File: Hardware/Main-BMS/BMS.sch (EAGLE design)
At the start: 131 parts, among them IC2 TLC6C5912-Q1, J1 SL03THROUGH_HOLE, J2 SL03THROUGH_HOLE, Q1 2N7002PW, Q11 2N7002PW, Q12 2N7002PW, Q13 2N7002PW, Q14 2N7002PW, Q15 2N7002PW, Q2 2N7002PW, Q3 2N7002PW, X1 22-23-2021, X2 22-23-2021, X3 22-23-2021, X4 22-23-2021, X5 22-23-2041, X6 22-23-2101, X7 22-23-2101

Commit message: Changed after board review
Made all changes suggested in pcb review, including several part
additions and complete rerouting.
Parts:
- removed D17, D18: BAT46W, SparkFun-DiscreteSemi:DIODE-ZENER16V
- removed S2: SWITCH-MOMENTARY-2SMD, SparkFun-Electromechanical:SWITCH-MOMENTARY-2SMD
- removed U$14: RJ45-8PTH, SparkFun-Connectors:RJ45-8PTH
- added D2, D24: BAT46WJ, diode:DIODE-SOD323-R
- added IC1: ACS759, MRDT-ICs:ACS759
- added R33: 200R, rcl:R-US_R0805
- added S1: SWITCH-MOMENTARY-2PTH, BMS:SWITCH-MOMENTARY-2PTH
- U$1: value ACS759 -> 5PIN; device MRDT-2017-BMS:ACS759 -> Molex-SL:5PIN
- U$13: value MSP432P401R-LAUNCHPAD -> MSP430R401R; device 2016PowerPackLibraries:MSP432P401R-LAUNCHPAD -> MRDT-Microcontrollers:MSP430R401R
- U$3: value Q_LTC6803-1 -> LTC6803-1; device MRDT-2017-BMS:Q_LTC6803-1 -> MRDT-ICs:LTC6803-1
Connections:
- removed net BMS_VREF: U$3.VREF
- removed net N$12: U$13.P3.3
- new net N$7: Q1.S, R33.2
- net +3V3: now also IC1.VCC; no longer U$1.VCC
- net 5V: now also Q3.D; no longer Q3.S
- net BMS_CSBI: now also U$13.P5.4; no longer U$13.P6.2
- net BMS_SCLK: now also U$13.P5.5; no longer U$13.P6.3
- net BUZZ_1: now also U$13.P4.7; no longer U$13.P8.6
- net CELL_8: now also IC1.IP-; no longer U$1.IP-
- net GAUGE_ON: now also S1.2, U$13.P4.6; no longer S2.2, U$13.P1.5
- net GND: now also D2.A, D24.A, IC1.GND, R33.1, S1.1, U$1.5; no longer D17.A, D18.A, Q1.S, S2.1, U$1.GND, U$14.7, U$14.8
- net LED_RCK: now also U$13.P3.3; no longer U$13.P6.1
- net LED_SER_IN: now also U$13.P1.5; no longer U$13.P4.3
- net LED_SRCK: now also U$13.P4.3; no longer U$13.P3.2
- net N$26: now also D2.C, D24.C; no longer D17.C, D18.C
- net N$35: now also U$1.1; no longer U$14.1
- net N$4: now also Q3.S; no longer Q3.D
- net N$41: now also IC1.IP+; no longer U$1.IP+
- net N$45: now also U$1.2; no longer U$14.2
- net N$62: now also U$1.4; no longer U$14.6
- net N$67: now also U$1.3; no longer U$14.3
- net PACK_GATE: now also U$13.P4.4; no longer U$13.P5.2
- net PACK_I_MEAS: now also IC1.VOUT, U$13.P6.0; no longer U$1.VIOUT, U$13.P4.5
- net TEMP_2: now also U$13.P5.6; no longer U$13.P3.5
- net V_CHECK_OUT: now also U$13.P4.5; no longer U$13.P4.4
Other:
- note removed: "BMS_VREF"
- note removed: "BMS_VREG"
- note removed: "CELL_1"
- note removed: "CELL_1_BAL"
- note removed: "CELL_1_FILTER"
- note removed: "CELL_2_BAL"
- note removed: "CELL_2_FILTER"
- note removed: "CELL_3_BAL"
- note removed: "CELL_3_FILTER"
- note removed: "CELL_4_BAL"
- note removed: "CELL_4_FILTER"
- note removed: "CELL_5_BAL"
- note removed: "CELL_5_FILTER"
- note removed: "CELL_6_BAL"
- note removed: "CELL_6_FILTER"
- note removed: "CELL_7_BAL"
- note removed: "CELL_7_FILTER"
- note removed: "CELL_8_BAL"
- note removed: "CELL_8_FILTER"
- moved on the sheet: V_ARRAY

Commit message: Changes for mountability
Changed GND terminal to Anderson connector, moved to opposite corner.
Changed package for current sensor, added connector for indicator
connection, swapped all data connectors for molex SLs
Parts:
- removed CELL-IN, CELL-MEAS: 22-23-2091, con-molex:22-23-2091
- removed GAUGE_ON: M02POLAR, SparkFun-Connectors:M02POLAR
- removed V_OUT1: TERMINAL_HOLE, MRDT-2015-PowerBoard:TERMINAL_HOLE
- removed X1, X2, X3, X4: 22-23-2021, con-molex:22-23-2021
- removed X6, X7: 22-23-2101, con-molex:22-23-2101
- added D4, D6: BZT52C15-7-F, SparkFun-DiscreteSemi:DIODE-ZENER16V
- added H1, H2, H3, H4: MOUNTING_HOLE#4, MRDT-Hardware:MOUNTING_HOLE#4
- added J3: APPPP45_PCB_VERT, MRDT-Connectors:APPPP45_PCB_VERT
- added U$10, U$11: SL10, MRDT-Connectors:SL10
- added U$12, U$14: SL09, MRDT-Connectors:SL09
- added U$16, U$2, U$5, U$6, U$7: SL02-VERT, MRDT-Connectors:SL02-VERT
- added U$18: SL04, MRDT-Connectors:SL04
- C21, C22: device resistor:C-USC1206 -> rcl:C-USC0805
- J1, J2: value SL03THROUGH_HOLE -> SL03; device MRDT-Connectors:SL03THROUGH_HOLE -> MRDT-Connectors:SL03
- R20, R40: device resistor:R-US_R1206 -> rcl:R-US_R0805
- R22, R57: device rcl:R-US_R1206 -> rcl:R-US_R0805
- R29, R30, R31, R32: value 10k -> 100k; device rcl:R-US_R1206 -> rcl:R-US_R0805
- U$1: value 5PIN -> SL05; device Molex-SL:5PIN -> MRDT-Connectors:SL05
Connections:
- removed net BUZZ_2: U$13.P8.5
- removed net SUPPLY_CTL: U$13.P2.3
- removed net SUPPLY_DC_OK: U$13.P1.7
- net 5V: now also U$18.3, U$2.1, U$5.1, U$6.1, U$7.1; no longer X1-2.S, X2-2.S, X3-2.S, X4-2.S
- net CELL_1: now also U$12.2, U$14.2; no longer CELL-IN-8.S, CELL-MEAS-8.S
- net CELL_2: now also U$12.3, U$14.3; no longer CELL-IN-7.S, CELL-MEAS-7.S
- net CELL_3: now also U$12.4, U$14.4; no longer CELL-IN-6.S, CELL-MEAS-6.S
- net CELL_4: now also U$12.5, U$14.5; no longer CELL-IN-5.S, CELL-MEAS-5.S
- net CELL_5: now also U$12.6, U$14.6; no longer CELL-IN-4.S, CELL-MEAS-4.S
- net CELL_6: now also U$12.7, U$14.7; no longer CELL-IN-3.S, CELL-MEAS-3.S
- net CELL_7: now also U$12.8, U$14.8; no longer CELL-IN-2.S, CELL-MEAS-2.S
- net CELL_8: now also IC1.IP+, U$12.9, U$14.9; no longer CELL-IN-1.S, CELL-MEAS-1.S, IC1.IP-
- net GAUGE_D: now also U$10.7; no longer X6-7.S
- net GAUGE_ON: now also U$16.2; no longer GAUGE_ON.2
- net GND: now also D4.A, D6.A, J3.P$1, U$12.1, U$14.1, U$16.1, U$18.4; no longer CELL-IN-9.S, CELL-MEAS-9.S, GAUGE_ON.1, V_OUT1.P$1
- net N$10: now also D4.C
- net N$13: now also D6.C
- net N$32: now also U$10.10; no longer X6-10.S
- net N$35: now also U$1.4, U$18.2; no longer U$1.1
- net N$41: now also IC1.IP-; no longer IC1.IP+
- net N$43: now also U$10.9; no longer X6-9.S
- net N$44: now also U$10.8; no longer X6-8.S
- net N$45: now also U$1.3, U$18.1; no longer U$1.2
- net N$46: now also U$10.6; no longer X6-6.S
- net N$47: now also U$10.5; no longer X6-5.S
- net N$48: now also U$10.4; no longer X6-4.S
- net N$49: now also U$10.3; no longer X6-3.S
- net N$50: now also U$10.2; no longer X6-2.S
- net N$51: now also U$10.1; no longer X6-1.S
- net N$62: now also U$1.2; no longer U$1.4
- net N$66: now also U$2.2; no longer X1-1.S
- net N$67: now also U$1.1; no longer U$1.3
- net N$70: now also U$5.2; no longer X2-1.S
- net N$71: now also U$6.2; no longer X3-1.S
- net N$72: now also U$7.2; no longer X4-1.S
- net N$75: now also U$11.1; no longer X7-1.S
- net N$76: now also U$11.2; no longer X7-2.S
- net N$77: now also U$11.3; no longer X7-3.S
- net N$78: now also U$11.4; no longer X7-4.S
- net N$79: now also U$11.5; no longer X7-5.S
- net N$80: now also U$11.6; no longer X7-6.S
- net N$81: now also U$11.7; no longer X7-7.S
- net N$82: now also U$11.8; no longer X7-8.S
- net N$83: now also U$11.9; no longer X7-9.S
- net N$84: now also U$11.10; no longer X7-10.S
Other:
- note added: "Communications connector"
- note added: "Indicator connector"
- note removed: "BMS_CSBI"
- note removed: "BMS_MISO"
- note removed: "BMS_MOSI"
- note removed: "BMS_SCLK"
- moved on the sheet: C18, IC1, R17, R18, R19, R21, R58, R59, R60, R61, R62, R63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

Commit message: DRC error fixes
Fixed several traces changed due to moving GND, and flipped signiture to
top.
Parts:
- R40: device rcl:R-US_R0805 -> rcl:R-US_R1206
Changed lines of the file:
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@@
 <part name="GND22" library="SparkFun-Aesthetics" deviceset="GND" device=""/>
 <part name="LED1" library="SparkFun-LED" deviceset="LED" device="1206"/>
-<part name="R40" library="rcl" deviceset="R-US_" device="R0805" value="5kΩ"/>
+<part name="R40" library="rcl" deviceset="R-US_" device="R1206" value="5kΩ"/>
 <part name="GND23" library="SparkFun-Aesthetics" deviceset="GND" device=""/>
 <part name="R41" library="resistor" deviceset="R-US_" device="R1206" value="100kΩ"/>

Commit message: Last changes after review
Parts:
- H1, H2, H3, H4: value MOUNTING_HOLE#4 -> MOUNTING_HOLE#6; device MRDT-Hardware:MOUNTING_HOLE#4 -> MRDT-Hardware:MOUNTING_HOLE#6
- renumbered J1 to TEMP_2, J2 to TEMP_1, JP2 to ESTOP_1, JP3 to ESTOP_2, U$1 to PB-COMM, U$10 to LED_SIG, U$11 to LED_PWR, U$18 to INDICATOR-COMM, U$2 to FAN_4, U$5 to FAN_3, U$6 to FAN_2, U$7 to FAN_1, V_ARRAY to V_IN
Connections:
- new net V_IN: IC1.IP+, V_IN.P$1
- net CELL_8: no longer IC1.IP+, V_IN.P$1

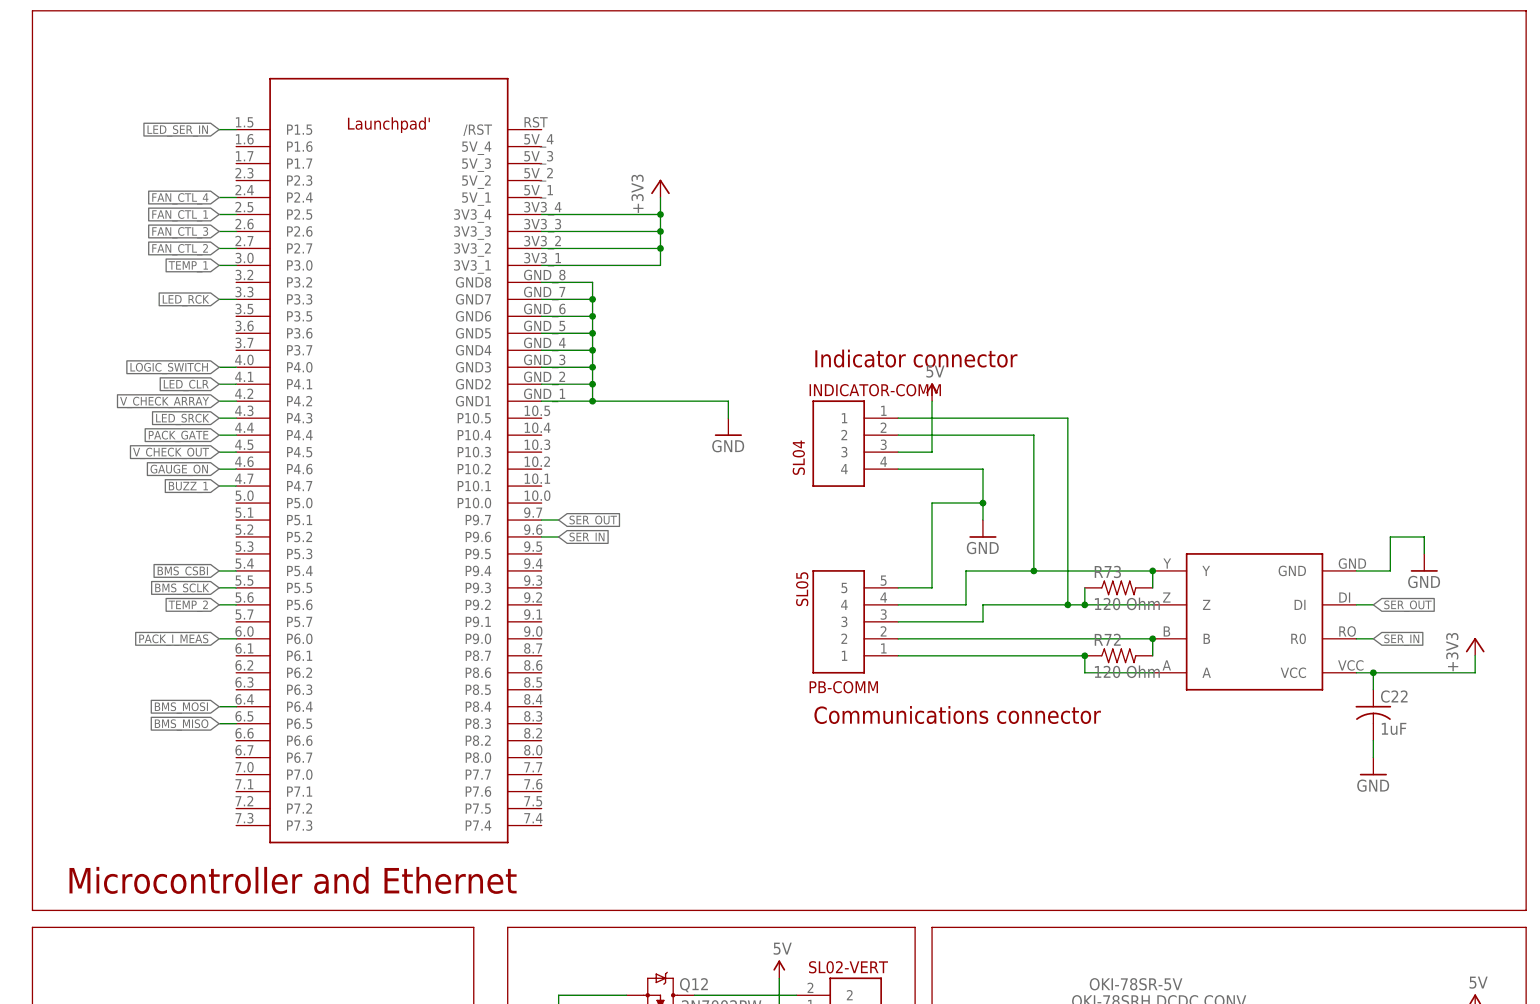
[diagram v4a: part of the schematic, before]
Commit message: Swapped RS485 for RS232
Changed MAX3077 (rs485) for MAX232. Indicator and Powerboard
communication now separate. Also rerouted LED driver and fan traces.
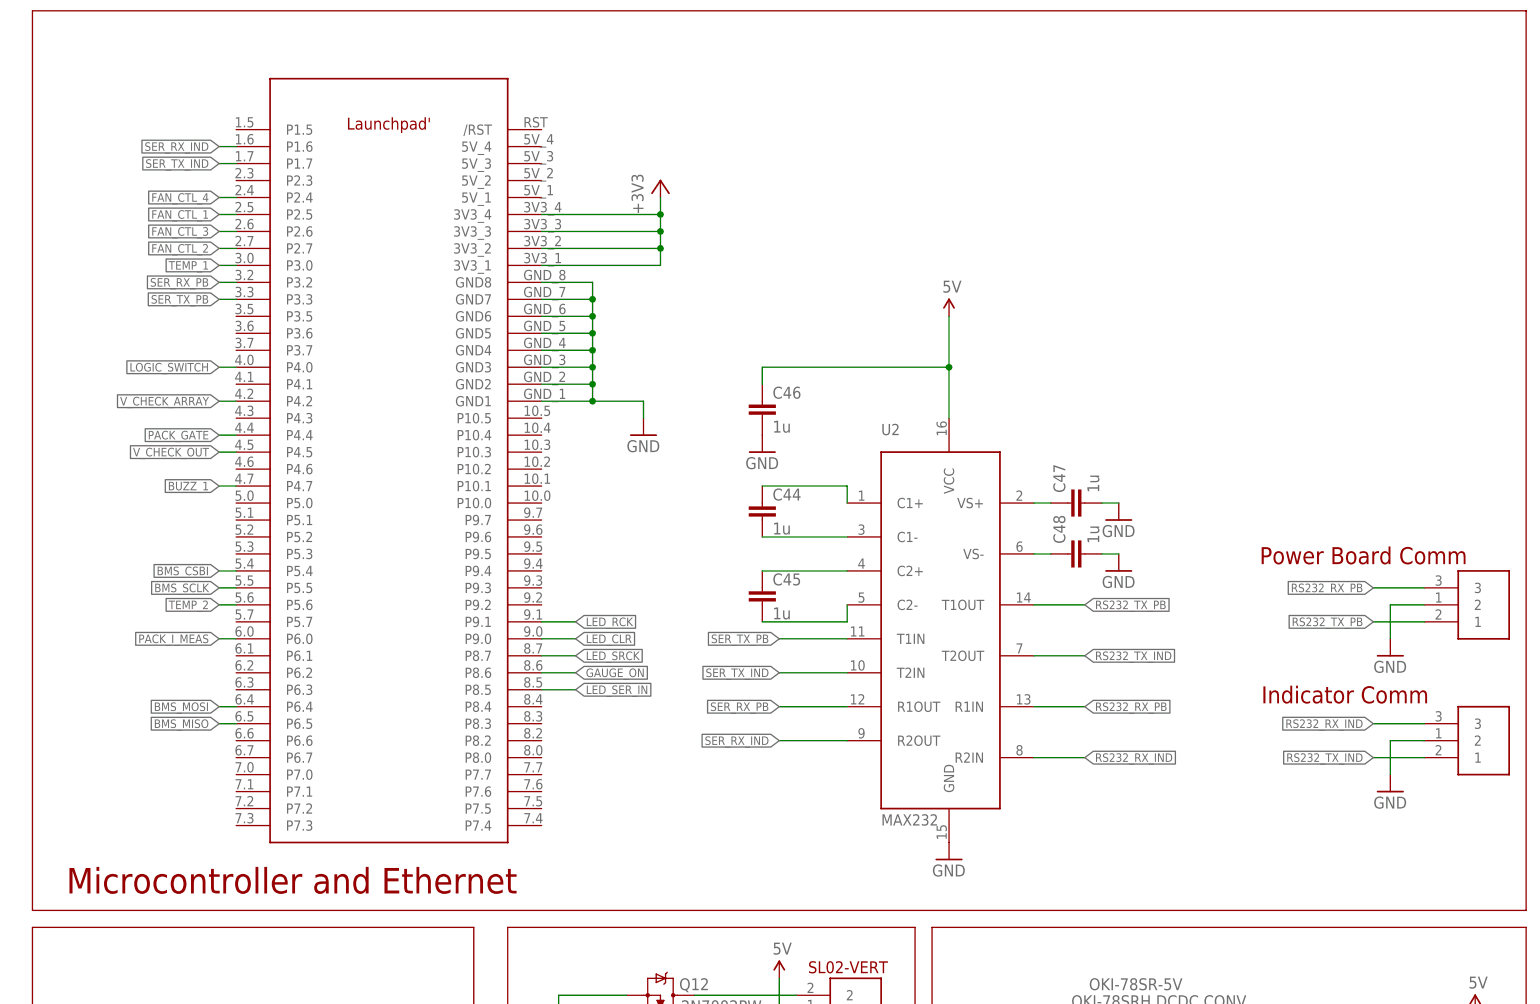
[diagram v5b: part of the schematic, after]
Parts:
- removed C22: 1uF, rcl:C-USC0805
- removed INDICATOR-COMM: SL04, MRDT-Connectors:SL04
- removed PB-COMM: SL05, MRDT-Connectors:SL05
- removed R72, R73: 120 Ohm, SparkFun-Passives:RESISTOR1206
- removed U$15: MAX3077, MAX3077:MAX3077
- added C44, C45, C46, C47, C48: 1u, SparkFun-Passives:CAP0805
- added RS232_IND, RS232_PB: SL03, MRDT-Connectors:SL03
- added U2: MAX232, MRDT-ICs:MAX232
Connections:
- removed net N$35: INDICATOR-COMM.2, PB-COMM.4, R73.2, U$15.Y
- removed net N$62: PB-COMM.2, R72.2, U$15.B
- removed net N$67: PB-COMM.1, R72.1, U$15.A
- removed net SER_IN: U$13.P9.6, U$15.R0
- removed net SER_OUT: U$13.P9.7, U$15.DI
- new net N$12: C45.2, U2.C2-
- new net N$14: C47.1, U2.VS+
- new net N$40: C44.1, U2.C1+
- new net N$42: C44.2, U2.C1-
- new net N$8: C45.1, U2.C2+
- new net RS232_RX_IND: RS232_IND.3, U2.R2IN
- new net RS232_RX_PB: RS232_PB.3, U2.R1IN
- new net RS232_TX_IND: RS232_IND.1, U2.T2OUT
- new net RS232_TX_PB: RS232_PB.1, U2.T1OUT
- new net SER_RX_IND: U$13.P1.6, U2.R2OUT
- new net SER_RX_PB: U$13.P3.2, U2.R1OUT
- new net SER_TX_IND: U$13.P1.7, U2.T2IN
- new net SER_TX_PB: U$13.P3.3, U2.T1IN
- net +3V3: no longer C22.1, U$15.VCC
- net 5V: now also C46.1, U2.VCC; no longer INDICATOR-COMM.3
- net GAUGE_ON: now also U$13.P8.6; no longer U$13.P4.6
- net GND: now also C46.2, C47.2, C48.2, RS232_IND.2, RS232_PB.2, U2.GND; no longer C22.2, INDICATOR-COMM.4, PB-COMM.5, U$15.GND
- net LED_CLR: now also U$13.P9.0; no longer U$13.P4.1
- net LED_RCK: now also U$13.P9.1; no longer U$13.P3.3
- net LED_SER_IN: now also U$13.P8.5; no longer U$13.P1.5
- net LED_SRCK: now also U$13.P8.7; no longer U$13.P4.3
- net N$45: now also C48.1, U2.VS-; no longer INDICATOR-COMM.1, PB-COMM.3, R73.1, U$15.Z
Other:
- note added: "Indicator Comm"
- note added: "Power Board Comm"
- note removed: "Communications connector"
- note removed: "Indicator connector"
